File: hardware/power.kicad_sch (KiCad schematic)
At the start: 10 parts, among them J1 173950578, J2 173950378, T2 PA2748NL

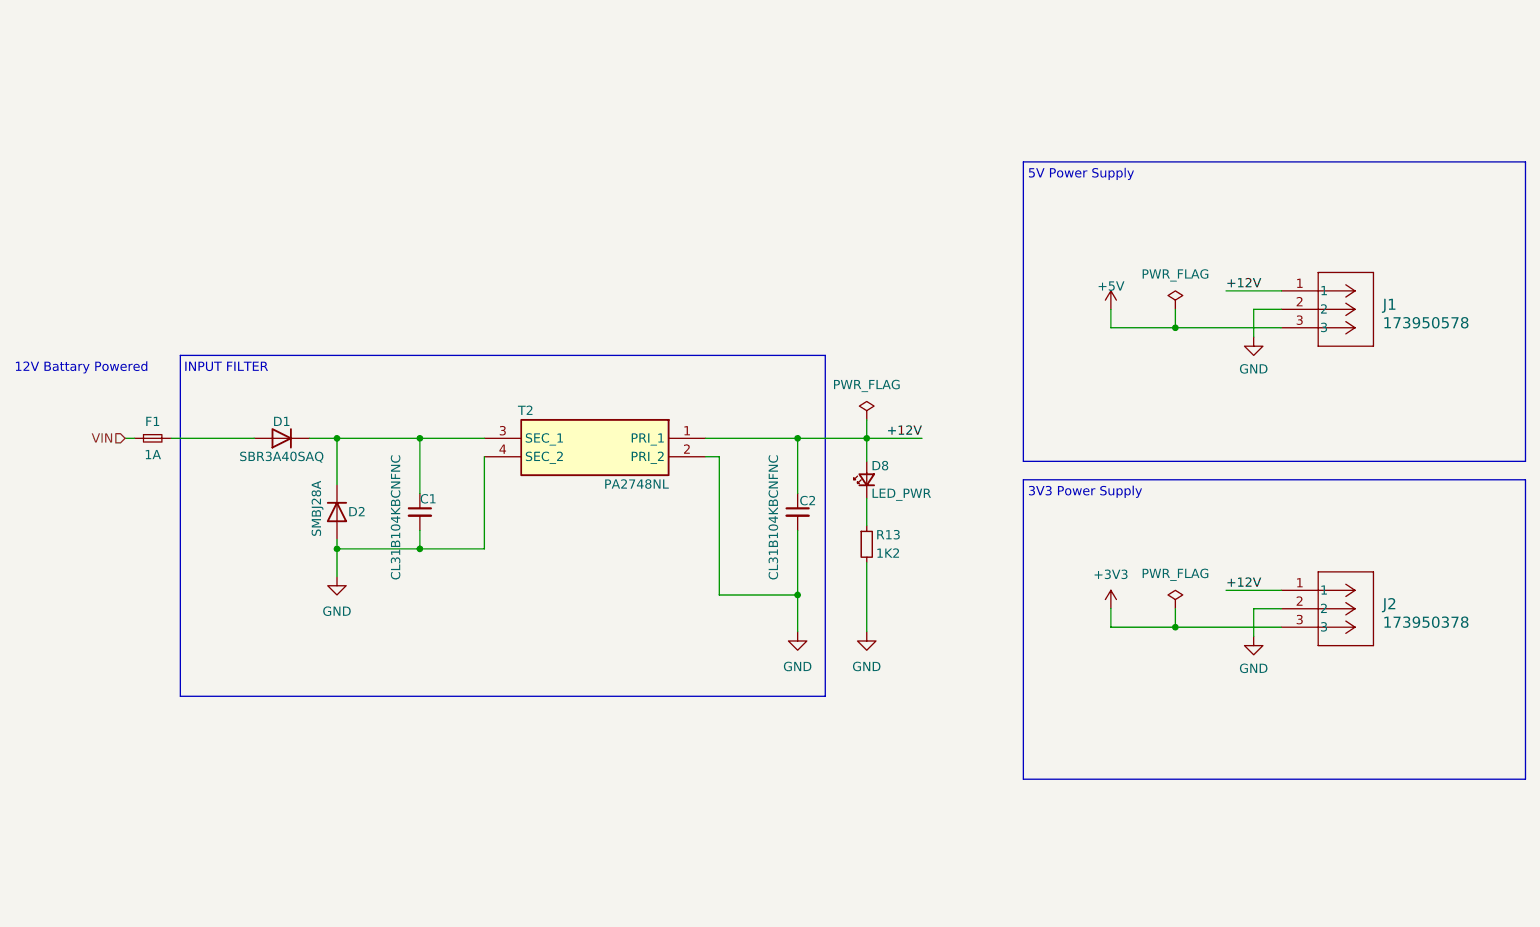
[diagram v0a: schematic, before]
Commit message: MCU BOOT0 mistake fixed
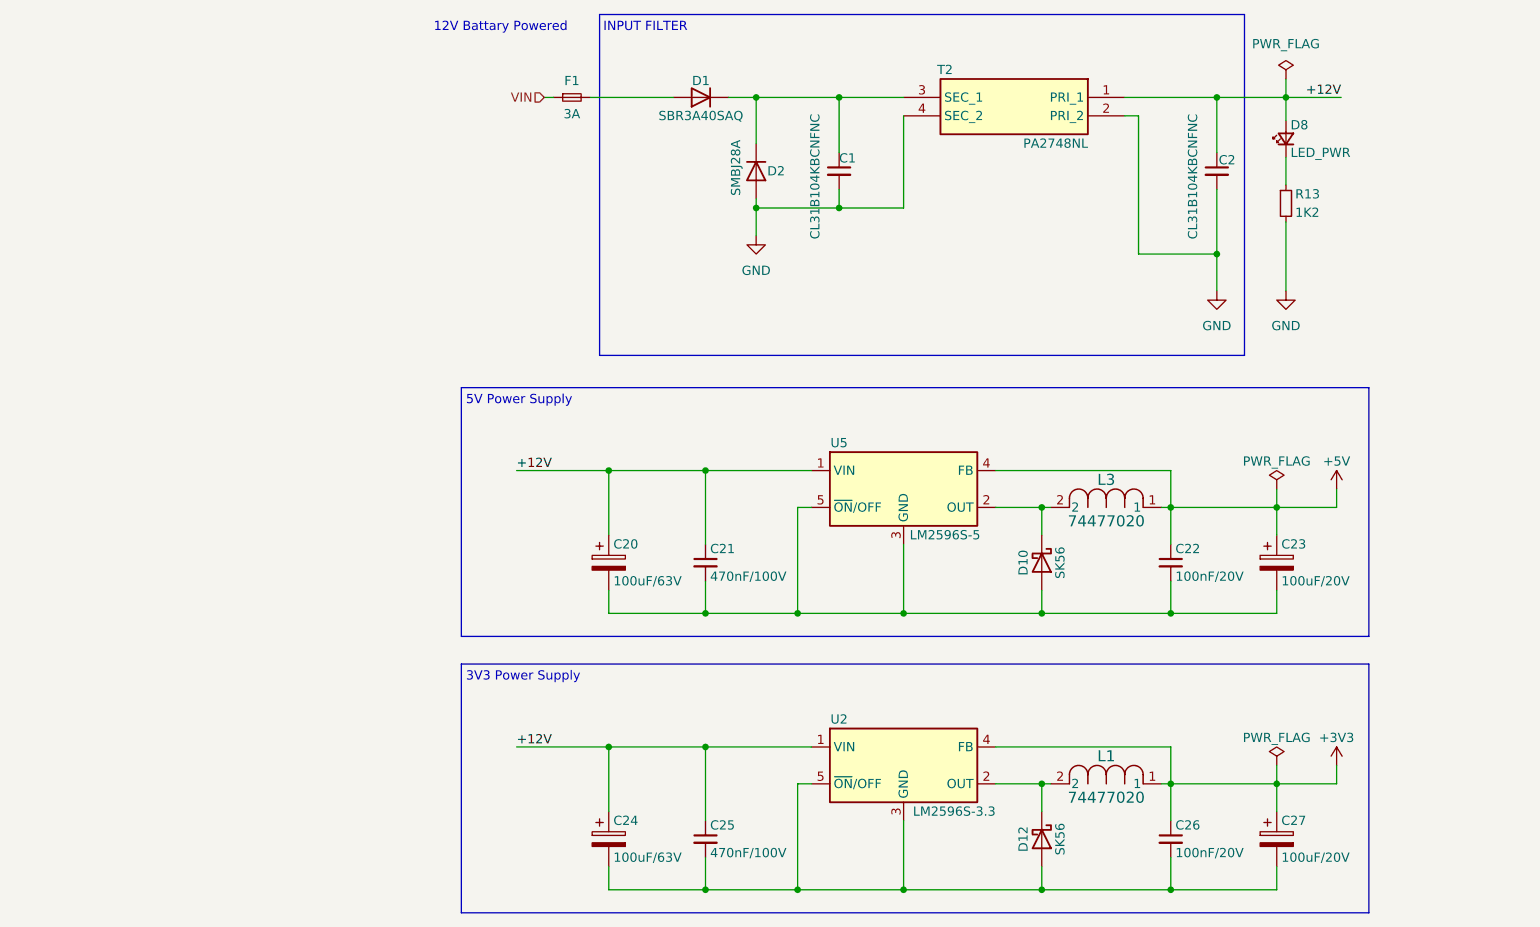
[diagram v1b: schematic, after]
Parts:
- removed J1: 173950578, Damlama:Wurth_Power_173950578, symbol Damlama:173950578
- removed J2: 173950378, Damlama:Wurth_Power_173950378, symbol Damlama:173950378
- added C20, C24: 100uF/63V, Capacitor_SMD:CP_Elec_10x10.5, symbol Device:C_Polarized
- added C21, C25: 470nF/100V, Capacitor_SMD:C_1206_3216Metric, symbol Device:C_Small
- added C22, C26: 100nF/20V, Capacitor_SMD:C_0805_2012Metric, symbol Device:C_Small
- added C23, C27: 100uF/20V, Capacitor_SMD:CP_Elec_6.3x7.7, symbol Device:C_Polarized
- added D10, D12: SK56, Diode_SMD:D_SMC, symbol Device:D_Schottky
- added L1, L3: 74477020, Damlama:IND_1280-WE-PD_WRE, symbol Damlama:74477020
- added U2: LM2596S-3.3, Package_TO_SOT_SMD:TO-263-5_TabPin3, symbol Regulator_Switching:LM2596S-3.3
- added U5: LM2596S-5, Package_TO_SOT_SMD:TO-263-5_TabPin3, symbol Regulator_Switching:LM2596S-5
- D2: footprint Diode_SMD:D_SMA -> Diode_SMD:D_SMB; DigikeyPN SMBJ28ALFTR-ND -> SMBJ28ALFDKR-ND
- D8: DigikeyPN (none) -> 1830-1004-ND
- F1: value 1A -> 3A; DigikeyPN P15124DKR-ND -> P16741DKR-ND
- R13: DigikeyPN (none) -> 13-RC0603FR-131K2LDKR-ND
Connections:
- net +12V: now also C20.1, C21.1, C24.1, C25.1, U2.1 (VIN), U5.1 (VIN)
- net +3V3: now also C26.1, C27.1, L1.1, U2.4 (FB)
- net +5V: now also C22.1, C23.1, L3.1, U5.4 (FB)
- new net: C24.2, C25.2, C26.2, C27.2, D12.2 (A), U2.3 (GND), U2.5 (~{ON}/OFF)
- new net: D10.1 (K), L3.2, U5.2 (OUT)
- new net: C20.2, C21.2, C22.2, C23.2, D10.2 (A), U5.3 (GND), U5.5 (~{ON}/OFF)
- new net: D12.1 (K), L1.2, U2.2 (OUT)
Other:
- moved on the sheet: C1, C2, D1, D2, D8, F1, R13, T2
